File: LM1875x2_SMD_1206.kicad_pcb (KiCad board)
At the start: 2 copper layers, 82.5 x 45 mm, 36 parts, among them J1 INPUT, J2 OUTPUT, J3 POWER, J4 VCC, J5 GND, J6 VEE, J7 SPK, J8 GND, U1 LM1875, U2 LM1875

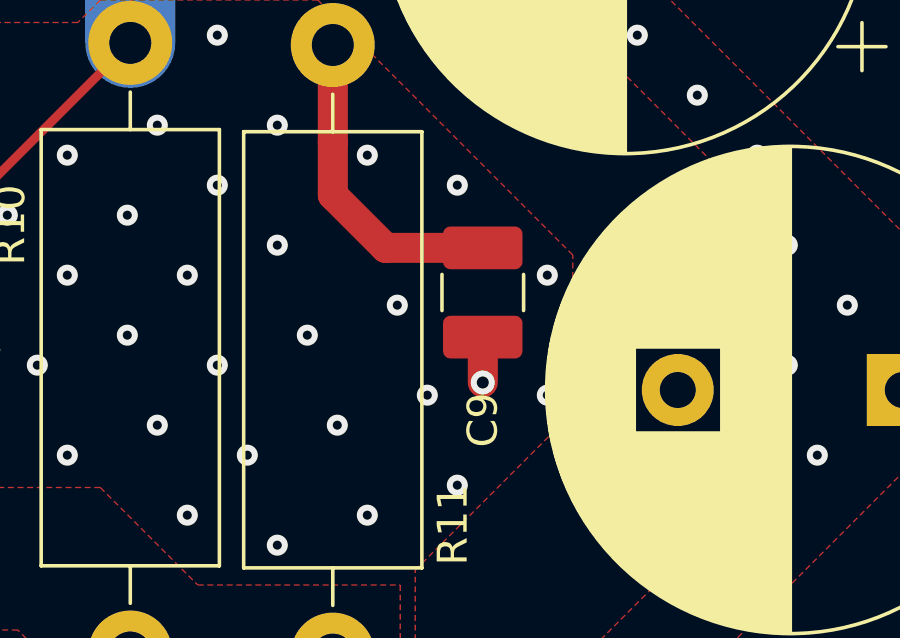
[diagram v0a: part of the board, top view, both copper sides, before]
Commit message: updated film cap footprint
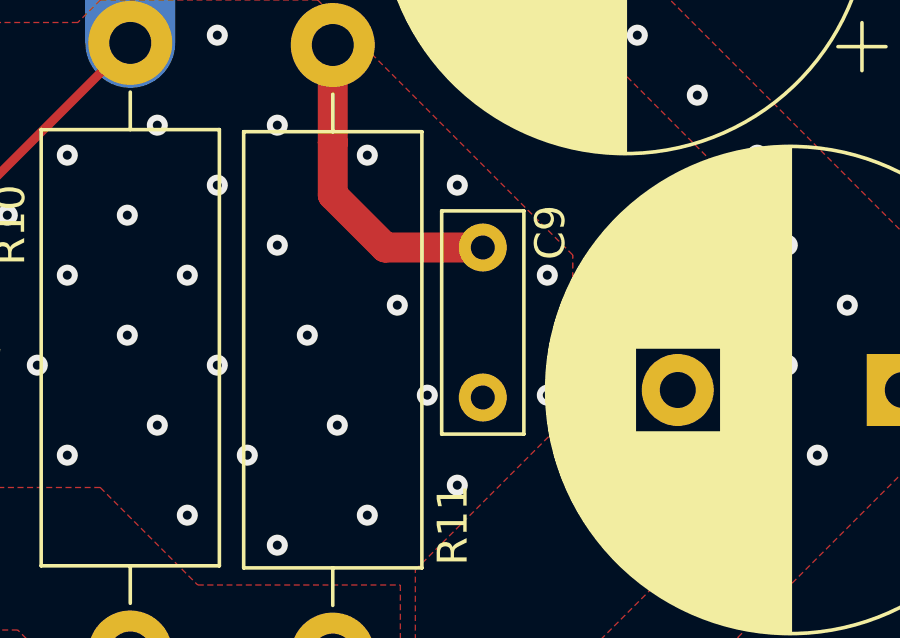
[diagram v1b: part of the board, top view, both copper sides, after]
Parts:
- C9: footprint Capacitor_SMD:C_1210_3225Metric_Pad1.42x2.65mm_HandSolder -> Capacitor_THT:C_Rect_L7.2mm_W2.5mm_P5.00mm_FKS2_FKP2_MKS2_MKP2
- moved C9 1.50 mm to (143.0, 67.2)
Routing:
- net GND: track 13.2 -> 11.7 mm, vias 173 -> 172

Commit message: minor fixes
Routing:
- net Net-(C2-Pad2): track 15.6 -> 16.8 mm
- net Net-(C2-Pad1): track 38.0 -> 38.6 mm
- net GND: vias 172 -> 169
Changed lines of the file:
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@@
     (thickness 1.6)
     (drawings 19)
-    (tracks 248)
+    (tracks 249)
     (zones 0)
     (modules 36)
@@
   )
   (setup
-    (last_trace_width 1)
+    (last_trace_width 0.3)
     (user_trace_width 1)
     (user_trace_width 3)
@@
       (effects (font (size 1 1) (thickness 0.15)))
     )
-    (fp_text user %R (at 2.5 0 90) (layer F.Fab)
-      (effects (font (size 1 1) (thickness 0.15)))
-    )
     (fp_line (start -1.1 -1.25) (end -1.1 1.25) (layer F.Fab) (width 0.1))
     (fp_line (start -1.1 1.25) (end 6.1 1.25) (layer F.Fab) (width 0.1))
@@
     (fp_line (start 6.35 1.5) (end 6.35 -1.5) (layer F.CrtYd) (width 0.05))
     (fp_line (start 6.35 -1.5) (end -1.35 -1.5) (layer F.CrtYd) (width 0.05))
+    (fp_text user %R (at 2.5 0 90) (layer F.Fab)
+      (effects (font (size 1 1) (thickness 0.15)))
+    )
     (pad 2 thru_hole circle (at 5 0 270) (size 1.6 1.6) (drill 0.8) (layers *.Cu *.Mask)
       (net 5 GND))
@@
   (gr_line (start 82.5 51.25) (end 82.5 88.75) (layer Edge.Cuts) (width 0.05))
   (gr_line (start 161.25 47.5) (end 86.25 47.5) (layer Edge.Cuts) (width 0.05))
-  (segment (start 100.25 87.5) (end 94.75 82) (width 0.3) (layer F.Cu) (net 1))
-  (segment (start 94.75 82) (end 94.75 78.25) (width 0.3) (layer F.Cu) (net 1))
   (segment (start 95.5 77.5) (end 100 77.5) (width 0.3) (layer F.Cu) (net 1))
+  (segment (start 98.75 83.75) (end 94.75 79.75) (width 0.3) (layer F.Cu) (net 1))
   (segment (start 94.75 78.25) (end 95.5 77.5) (width 0.3) (layer F.Cu) (net 1))
+  (segment (start 98.75 86) (end 98.75 83.75) (width 0.3) (layer F.Cu) (net 1))
+  (segment (start 94.75 79.75) (end 94.75 78.25) (width 0.3) (layer F.Cu) (net 1))
+  (segment (start 100.25 87.5) (end 98.75 86) (width 0.3) (layer F.Cu) (net 1))
   (segment (start 118.54999 67.10001) (end 120.5 65.15) (width 0.3) (layer F.Cu) (net 2))
   (segment (start 99.95001 67.10001) (end 118.54999 67.10001) (width 0.3) (layer F.Cu) (net 2))
   (segment (start 98 65.15) (end 99.95001 67.10001) (width 0.3) (layer F.Cu) (net 2))
-  (segment (start 95.77499 66.22501) (end 95.5 66.5) (width 0.3) (layer F.Cu) (net 2))
-  (segment (start 96.02499 66.22501) (end 95.77499 66.22501) (width 0.3) (layer F.Cu) (net 2))
-  (segment (start 96.5 65.5) (end 96.5 65.75) (width 0.3) (layer F.Cu) (net 2))
-  (segment (start 96 72.5) (end 100 72.5) (width 0.3) (layer F.Cu) (net 2))
-  (segment (start 96.5 65.75) (end 96.02499 66.22501) (width 0.3) (layer F.Cu) (net 2))
-  (segment (start 96.85 65.15) (end 96.5 65.5) (width 0.3) (layer F.Cu) (net 2))
-  (segment (start 98 65.15) (end 96.85 65.15) (width 0.3) (layer F.Cu) (net 2))
-  (segment (start 95.5 72) (end 96 72.5) (width 0.3) (layer F.Cu) (net 2))
-  (segment (start 95.5 66.5) (end 95.5 72) (width 0.3) (layer F.Cu) (net 2))
+  (segment (start 95.350009 72.5) (end 100 72.5) (width 0.3) (layer F.Cu) (net 2))
+  (segment (start 94.850009 72) (end 95.350009 72.5) (width 0.3) (layer F.Cu) (net 2))
+  (segment (start 94.850009 69.899991) (end 94.850009 72) (width 0.3) (layer F.Cu) (net 2))
+  (segment (start 96.75 68) (end 94.850009 69.899991) (width 0.3) (layer F.Cu) (net 2))
+  (segment (start 96.75 66.25) (end 96.75 68) (width 0.3) (layer F.Cu) (net 2))
+  (segment (start 97.85 65.15) (end 96.75 66.25) (width 0.3) (layer F.Cu) (net 2))
+  (segment (start 98 65.15) (end 97.85 65.15) (width 0.3) (layer F.Cu) (net 2))
   (segment (start 92.75 77.5) (end 89.25 77.5) (width 0.3) (layer F.Cu) (net 3))
   (segment (start 93.5 77.5) (end 92.75 77.5) (width 0.3) (layer F.Cu) (net 3))
-  (segment (start 94.14999 82.248532) (end 94.14999 78.14999) (width 0.3) (layer F.Cu) (net 3))
   (segment (start 94.14999 78.14999) (end 93.5 77.5) (width 0.3) (layer F.Cu) (net 3))
-  (segment (start 96.75 84.848542) (end 94.14999 82.248532) (width 0.3) (layer F.Cu) (net 3))
-  (segment (start 96.75 87.5) (end 96.75 84.848542) (width 0.3) (layer F.Cu) (net 3))
-  (segment (start 94.89999 65.25001) (end 95 65.15) (width 0.3) (layer F.Cu) (net 4))
-  (segment (start 94.89999 72.10001) (end 94.89999 65.25001) (width 0.3) (layer F.Cu) (net 4))
-  (segment (start 94.5 72.5) (end 94.89999 72.10001) (width 0.3) (layer F.Cu) (net 4))
-  (segment (start 89.25 72.5) (end 94.5 72.5) (width 0.3) (layer F.Cu) (net 4))
+  (segment (start 94.14999 79.998532) (end 94.14999 78.14999) (width 0.3) (layer F.Cu) (net 3))
+  (segment (start 98.14999 83.998532) (end 94.14999 79.998532) (width 0.3) (layer F.Cu) (net 3))
+  (segment (start 98.14999 86.10001) (end 98.14999 83.998532) (width 0.3) (layer F.Cu) (net 3))
+  (segment (start 96.75 87.5) (end 98.14999 86.10001) (width 0.3) (layer F.Cu) (net 3))
   (segment (start 98.914956 64.07499) (end 99.5 64.660034) (width 0.3) (layer F.Cu) (net 4))
   (segment (start 96.07501 64.07499) (end 98.914956 64.07499) (width 0.3) (layer F.Cu) (net 4))
@@
   (segment (start 116.15 66.5) (end 117.5 65.15) (width 0.3) (layer F.Cu) (net 4))
   (segment (start 100.198542 66.5) (end 116.15 66.5) (width 0.3) (layer F.Cu) (net 4))
+  (segment (start 95.15 65.15) (end 95 65.15) (width 0.3) (layer F.Cu) (net 4))
+  (segment (start 96.149991 66.149991) (end 95.15 65.15) (width 0.3) (layer F.Cu) (net 4))
+  (segment (start 94.25 72) (end 94.25 69.651458) (width 0.3) (layer F.Cu) (net 4))
+  (segment (start 94.25 69.651458) (end 96.149991 67.751467) (width 0.3) (layer F.Cu) (net 4))
+  (segment (start 93.75 72.5) (end 94.25 72) (width 0.3) (layer F.Cu) (net 4))
+  (segment (start 96.149991 67.751467) (end 96.149991 66.149991) (width 0.3) (layer F.Cu) (net 4))
+  (segment (start 89.25 72.5) (end 93.75 72.5) (width 0.3) (layer F.Cu) (net 4))
   (segment (start 107.475 54.0125) (end 107.5 53.9875) (width 1) (layer F.Cu) (net 5))
   (segment (start 105 54.0125) (end 107.475 54.0125) (width 1) (layer F.Cu) (net 5))
@@
   (via (at 96.151191 90.1725) (size 0.7) (drill 0.3) (layers F.Cu B.Cu) (net 5))
   (via (at 97.151191 49.1725) (size 0.7) (drill 0.3) (layers F.Cu B.Cu) (net 5))
-  (via (at 97.151191 67.1725) (size 0.7) (drill 0.3) (layers F.Cu B.Cu) (net 5))
   (via (at 97.151191 71.1725) (size 0.7) (drill 0.3) (layers F.Cu B.Cu) (net 5))
-  (via (at 97.151191 82.1725) (size 0.7) (drill 0.3) (layers F.Cu B.Cu) (net 5))
   (via (at 98.151191 76.1725) (size 0.7) (drill 0.3) (layers F.Cu B.Cu) (net 5))
   (via (at 99.151191 69.1725) (size 0.7) (drill 0.3) (layers F.Cu B.Cu) (net 5))
   (via (at 99.151191 80.1725) (size 0.7) (drill 0.3) (layers F.Cu B.Cu) (net 5))
-  (via (at 99.151191 84.1725) (size 0.7) (drill 0.3) (layers F.Cu B.Cu) (net 5))
   (via (at 99.151191 91.1725) (size 0.7) (drill 0.3) (layers F.Cu B.Cu) (net 5))
   (via (at 101.151191 75.1725) (size 0.7) (drill 0.3) (layers F.Cu B.Cu) (net 5))
